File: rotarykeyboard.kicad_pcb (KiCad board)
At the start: 2 copper layers, 53 parts, among them J101 Breakout, J102 Cortex Debug, J301 USB_C_Receptacle_USB2.0, SW101 RotaryEncoder, SW102 KBPush, SW103 RESET, U101 ATSAMDA1E14B-ABT, U201 QS6K1FRATR, U202 LTP-3784E, U203 PCA9685PW, U301 FTZU6.2ET148, U302 XC9265A331MR-G

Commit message: finish routing(?)
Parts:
- added REF**: MountingHole_2.2mm_M2_ISO7380, MountingHole:MountingHole_2.2mm_M2_ISO7380, F.Cu at (106.7, 40.6)
- added REF**: MountingHole_2.2mm_M2_ISO7380, MountingHole:MountingHole_2.2mm_M2_ISO7380, F.Cu at (106.7, 113.0)
- added REF**: MountingHole_2.2mm_M2_ISO7380, MountingHole:MountingHole_2.2mm_M2_ISO7380, F.Cu at (62.2, 40.6)
- added REF**: MountingHole_2.2mm_M2_ISO7380, MountingHole:MountingHole_2.2mm_M2_ISO7380, F.Cu at (62.2, 113.0)
- moved R203 25.2 mm to (63.8, 99.3), turned to -90 degrees
- moved R204 20.9 mm to (63.8, 94.7), turned to -90 degrees
- moved R212 18.8 mm to (81.5, 85.3), turned to -90 degrees
- moved R215 15.3 mm to (78.0, 89.9), turned to -90 degrees
- moved R210 14.2 mm to (81.5, 80.8), turned to -90 degrees
- moved R207 12.7 mm to (63.8, 89.9), turned to -90 degrees
- moved R208 11.1 mm to (63.8, 85.3), turned to -90 degrees
- moved R214 10.9 mm to (81.5, 89.9), turned to -90 degrees
- moved R213 10.7 mm to (78.0, 85.3), turned to -90 degrees
- moved U203 10.4 mm to (70.9, 79.2), turned to 0 degrees
- moved R209 9.77 mm to (67.3, 89.9), turned to -90 degrees
- moved U201 9.51 mm to (89.3, 90.4), turned to -90 degrees
- moved R205 8.13 mm to (63.8, 74.4), turned to -90 degrees
- moved R216 7.28 mm to (74.4, 89.9), turned to -90 degrees
- moved R211 6.13 mm to (78.0, 80.8), turned to -90 degrees
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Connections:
- R203 pad 1: Net-(R203-Pad1) -> Net-(U203-Pad6)
- R203 pad 2: Net-(R203-Pad2) -> Net-(U202-Pad1)
- R204 pad 1: Net-(R204-Pad1) -> Net-(U203-Pad7)
- R204 pad 2: Net-(R204-Pad2) -> Net-(U202-Pad2)
- R205 pad 1: Net-(R205-Pad1) -> Net-(U203-Pad8)
- R206 pad 1: Net-(R206-Pad1) -> Net-(U203-Pad9)
- R206 pad 2: Net-(R206-Pad2) -> Net-(U202-Pad5)
- R207 pad 1: Net-(R207-Pad1) -> Net-(U203-Pad10)
- R207 pad 2: Net-(R207-Pad2) -> Net-(U202-Pad6)
- R208 pad 1: Net-(R208-Pad1) -> Net-(U203-Pad11)
- R209 pad 1: Net-(R209-Pad1) -> Net-(U203-Pad12)
- U202 pad 1: Net-(R203-Pad1) -> Net-(U202-Pad1)
- U202 pad 2: Net-(R204-Pad1) -> Net-(U202-Pad2)
- U202 pad 4: Net-(R205-Pad1) -> Net-(R205-Pad2)
- U202 pad 5: Net-(R206-Pad1) -> Net-(U202-Pad5)
- U202 pad 6: Net-(R207-Pad1) -> Net-(U202-Pad6)
- U202 pad 7: Net-(R208-Pad1) -> Net-(R208-Pad2)
- U202 pad 8: Net-(R209-Pad1) -> Net-(R209-Pad2)
- U203 pad 10: Net-(R207-Pad2) -> Net-(U203-Pad10)
- U203 pad 11: Net-(R208-Pad2) -> Net-(U203-Pad11)
- U203 pad 12: Net-(R209-Pad2) -> Net-(U203-Pad12)
- U203 pad 6: Net-(R203-Pad2) -> Net-(U203-Pad6)
- U203 pad 7: Net-(R204-Pad2) -> Net-(U203-Pad7)
- U203 pad 8: Net-(R205-Pad2) -> Net-(U203-Pad8)
- U203 pad 9: Net-(R206-Pad2) -> Net-(U203-Pad9)
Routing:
- net Net-(R205-Pad2): track 0.00 -> 47.7 mm, vias 0 -> 1
- net Net-(U202-Pad5): track 0.00 -> 44.9 mm, vias 0 -> 1
- net Net-(R208-Pad2): track 0.00 -> 41.2 mm, vias 0 -> 1
- net GND: track 170.2 -> 211.0 mm, vias 9 -> 12
- net Net-(R217-Pad2): track 0.00 -> 39.1 mm, vias 0 -> 1
- net Net-(R209-Pad2): track 0.00 -> 37.3 mm, vias 0 -> 1
- net Net-(U202-Pad6): track 0.00 -> 34.5 mm, vias 0 -> 1
- net Net-(R216-Pad2): track 0.00 -> 33.3 mm
- net Net-(R211-Pad2): track 0.00 -> 31.0 mm, vias 0 -> 1
- net Net-(U203-Pad6): track 0.00 -> 29.8 mm
- net Net-(R210-Pad2): track 0.00 -> 29.0 mm
- net Net-(U201-Pad4): track 32.0 -> 5.27 mm
- net Net-(U203-Pad7): track 0.00 -> 24.4 mm
- net Net-(R101-Pad2): track 30.0 -> 53.3 mm
- net Net-(U202-Pad2): track 0.00 -> 22.1 mm, vias 0 -> 1
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- added copper zone on B.Cu, net +3V3
- removed copper zone on F.Cu, net +5V
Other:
- board outline added: 49.5 x 77.5 mm
- board text removed: "roter LED-driveren 90 grader flytt displaymotstandene til hver sin side av driveren"

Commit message: replace out of stock components
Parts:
- added C201: 0.1u, Capacitor_SMD:C_0805_2012Metric, F.Cu at (133.3, 82.5)
- added R210: 100k, Resistor_SMD:R_0805_2012Metric, F.Cu at (137.8, 82.5)
- added R219: 6k8, Resistor_SMD:R_0805_2012Metric, F.Cu at (133.3, 85.5)
- U203: value PCA9685PW -> IS32FL3238
- U301: value FTZU6.2ET148 -> BZA856AVL; footprint FTZU6.2ET148:FTZU6.2ET148 -> BZA856AVL:BZA856AVL
- moved U301 45.2 mm to (117.9, 86.9), turned to 0 degrees
- renumbered C106 to C101, C107 to C102, C101 to C103, C102 to C104, C103 to C105, C104 to C106, C105 to C107, R210 to R211, R211 to R212, R212 to R213, R213 to R214, R214 to R215, R215 to R216, R216 to R217, R217 to R218, GND to TP301, +3V3 to TP302
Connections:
- R203 pad 1: Net-(U203-Pad6) -> Net-(R203-Pad1)
- R204 pad 1: Net-(U203-Pad7) -> Net-(R204-Pad1)
- R205 pad 1: Net-(U203-Pad8) -> Net-(R205-Pad1)
- R206 pad 1: Net-(U203-Pad9) -> Net-(R206-Pad1)
- R207 pad 1: Net-(U203-Pad10) -> Net-(R207-Pad1)
- R208 pad 1: Net-(U203-Pad11) -> Net-(R208-Pad1)
- R209 pad 1: Net-(U203-Pad12) -> Net-(R209-Pad1)
- R217 pad 1: Net-(R216-Pad1) (its old number) -> Net-(R217-Pad1)
- R218 pad 1: Net-(R217-Pad1) -> Net-(R218-Pad1)
- U101 pad 13: /Segment display/~OE -> /Segment display/EN
- U201 pad 2: GND -> Net-(U201-Pad2)
- U201 pad 4: Net-(U201-Pad4) -> +3V3
- U201 pad 5: GND -> Net-(U201-Pad5)
- U201 pad 6: Net-(U201-Pad6) -> +3V3
- U202 pad 11: Net-(U201-Pad4) -> Net-(U201-Pad2)
- U202 pad 16: Net-(U201-Pad6) -> Net-(U201-Pad5)
- U203 pad 1: +3V3 -> (no net)
- U203 pad 10: Net-(U203-Pad10) -> Net-(R208-Pad1)
- U203 pad 11: Net-(U203-Pad11) -> Net-(R209-Pad1)
- U203 pad 12: Net-(U203-Pad12) -> Net-(R218-Pad1)
- U203 pad 15: Net-(R216-Pad1) (its old number) -> GND
- U203 pad 2: GND -> Net-(R219-Pad1)
- U203 pad 23: /Segment display/~OE -> unconnected-(U203-Pad23)
- U203 pad 24: GND -> unconnected-(U203-Pad24)
- U203 pad 25: GND -> /Segment display/EN
- U203 pad 26: /Segment display/SCL -> +3V3
- U203 pad 27: /Segment display/SDA -> +3V3
- U203 pad 28: +3V3 -> GND
- U203 pad 3: +3V3 -> /Segment display/SDA
- U203 pad 4: GND -> /Segment display/SCL
- U203 pad 5: +3V3 -> Net-(R203-Pad1)
- U203 pad 6: Net-(U203-Pad6) -> Net-(R204-Pad1)
- U203 pad 7: Net-(U203-Pad7) -> Net-(R205-Pad1)
- U203 pad 8: Net-(U203-Pad8) -> Net-(R206-Pad1)
- U203 pad 9: Net-(U203-Pad9) -> Net-(R207-Pad1)
- U301 pad 1: /USB & Power/USB_D+ -> unconnected-(U301-Pad1)
- U301 pad 2: /USB & Power/USB_D- -> Net-(C301-Pad1)
- U301 pad 4: Net-(C301-Pad1) -> /USB & Power/USB_D-
- U301 pad 5: unconnected-(U301-Pad5) -> /USB & Power/USB_D+
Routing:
- net unconnected-(U203-Pad23): track 0.00 -> 32.7 mm
- net /Segment display/~OE: track 32.7 -> 0.00 mm
- net Net-(U203-Pad6): track 29.8 -> 0.00 mm
- net Net-(R203-Pad1): track 0.00 -> 29.8 mm
- net Net-(U203-Pad7): track 24.4 -> 0.00 mm
- net Net-(R205-Pad1): track 0.00 -> 24.4 mm
- net Net-(U201-Pad6): track 20.7 -> 0.00 mm, vias 2 -> 0
- net Net-(U201-Pad5): track 0.00 -> 20.7 mm, vias 0 -> 2
- net Net-(U203-Pad12): track 12.9 -> 0.00 mm, vias 2 -> 0
- net Net-(R218-Pad1): track 0.00 -> 12.9 mm, vias 0 -> 2
- net Net-(U203-Pad10): track 12.6 -> 0.00 mm
- net Net-(R208-Pad1): track 0.00 -> 12.6 mm
- net Net-(U203-Pad8): track 12.4 -> 0.00 mm
- net Net-(R206-Pad1): track 0.00 -> 12.4 mm
- net Net-(U203-Pad9): track 8.09 -> 0.00 mm
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
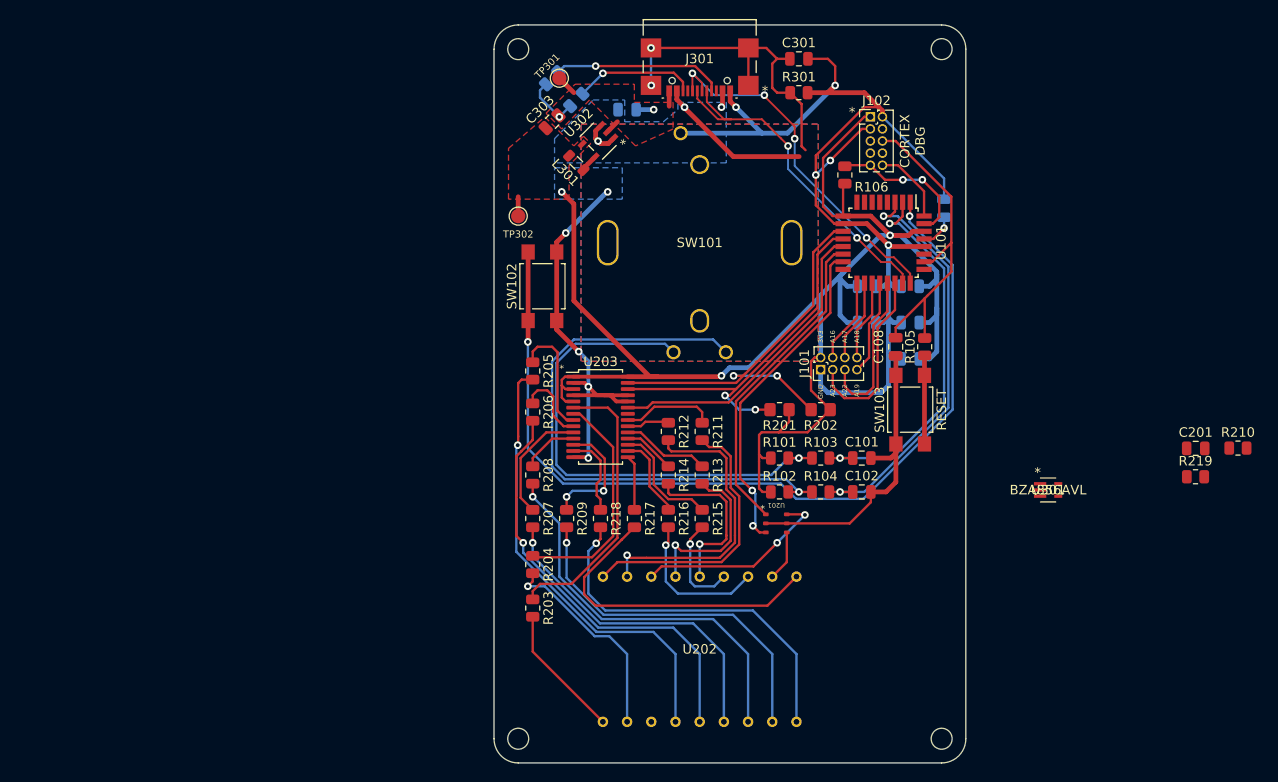
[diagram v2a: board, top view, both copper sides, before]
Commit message: reroute new components
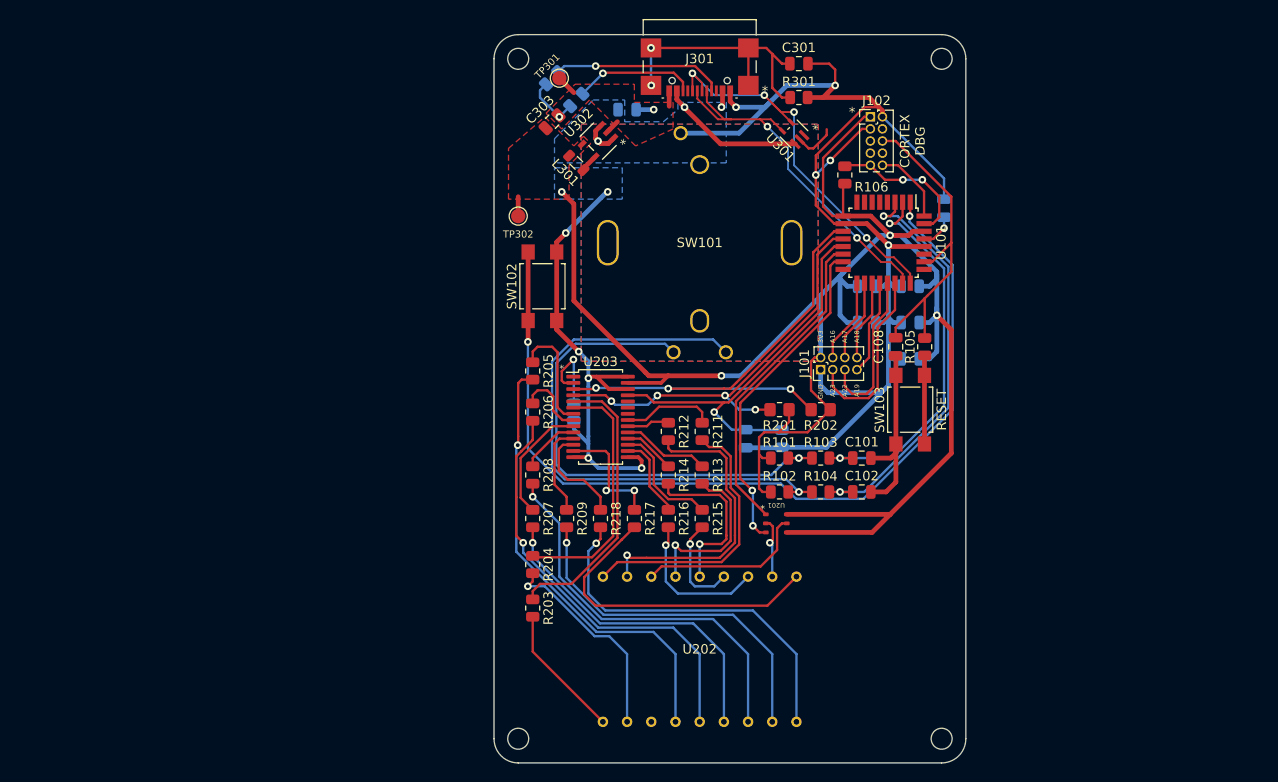
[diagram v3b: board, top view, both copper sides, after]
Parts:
- C201, R210: moved to B.Cu
- R219: value 6k8 -> 10k; moved to B.Cu
- moved R219 65.6 mm to (68.1, 78.7), turned to -90 degrees
- moved R210 47.9 mm to (89.9, 81.5), turned to -90 degrees
- moved C201 47.3 mm to (86.1, 81.5), turned to -90 degrees
- moved U301 45.9 mm to (91.2, 49.5), turned to -45 degrees
- moved REF** 1.02 mm to (106.7, 41.7)
- moved REF** 1.02 mm to (62.2, 41.7)
- moved C301 0.51 mm to (91.7, 42.2)
- moved R301 0.51 mm to (91.7, 45.7)
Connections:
- U203 pad 26: +3V3 -> GND
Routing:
- net /Segment display/EN: track 0.00 -> 42.2 mm, vias 0 -> 1
- net +3V3: track 163.7 -> 200.0 mm, vias 3 -> 4
- net unconnected-(U203-Pad23): track 32.7 -> 0.00 mm
- net Net-(R204-Pad1): track 0.00 -> 26.4 mm
- net Net-(R205-Pad1): track 24.4 -> 11.9 mm
- net /Segment display/SDA: track 43.5 -> 54.8 mm, vias 2 -> 3
- net Net-(R219-Pad1): track 0.00 -> 8.66 mm, vias 0 -> 1
- net Net-(R208-Pad1): track 12.6 -> 6.24 mm
- net /Segment display/SCL: track 39.2 -> 44.6 mm, vias 2 -> 4
- net Net-(R206-Pad1): track 12.4 -> 7.52 mm
- net Net-(R207-Pad1): track 8.09 -> 12.9 mm
- net GND: track 216.9 -> 220.9 mm, vias 12 -> 13
- net Net-(R217-Pad1): track 8.79 -> 12.8 mm, vias 0 -> 2
- net /USB & Power/USB_D+: track 39.2 -> 43.0 mm
- net Net-(R209-Pad1): track 5.97 -> 9.67 mm
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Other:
- board size 49.5 x 77.5 mm -> 49.5 x 76.5 mm

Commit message: påske
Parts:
- removed R203, R204, R205, R206, R207, R208, R209, R211, R212, R213, R214, R215, R216, R217, R218: 330, Resistor_SMD:R_0805_2012Metric
- U202: value LTP-3784E -> XAMR14A2
- moved U201 12.7 mm to (80.3, 81.5), turned to 180 degrees
- moved U202 3.56 mm to (81.3, 100.1)
- moved REF** 2.16 mm to (106.7, 110.9)
- moved REF** 2.16 mm to (62.2, 110.9)
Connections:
- U202 pad 1: Net-(R203-Pad2) -> Net-(U203-Pad5)
- U202 pad 10: Net-(R217-Pad2) -> Net-(U203-Pad13)
- U202 pad 11: Net-(U201-Pad2) -> Net-(U201-Pad5)
- U202 pad 12: Net-(R216-Pad2) -> Net-(U203-Pad16)
- U202 pad 13: Net-(R215-Pad2) -> Net-(U203-Pad17)
- U202 pad 14: Net-(R214-Pad2) -> Net-(U203-Pad18)
- U202 pad 15: Net-(R213-Pad2) -> Net-(U203-Pad19)
- U202 pad 16: Net-(U201-Pad5) -> Net-(U201-Pad2)
- U202 pad 17: Net-(R212-Pad2) -> Net-(U203-Pad20)
- U202 pad 18: Net-(R211-Pad2) -> Net-(U203-Pad21)
- U202 pad 2: Net-(R204-Pad2) -> Net-(U203-Pad6)
- U202 pad 4: Net-(R205-Pad2) -> Net-(U203-Pad7)
- U202 pad 5: Net-(R206-Pad2) -> Net-(U203-Pad8)
- U202 pad 6: Net-(R207-Pad2) -> Net-(U203-Pad9)
- U202 pad 7: Net-(R208-Pad2) -> Net-(U203-Pad10)
- U202 pad 8: Net-(R209-Pad2) -> Net-(U203-Pad11)
- U202 pad 9: Net-(R218-Pad2) -> Net-(U203-Pad12)
- U203 pad 10: Net-(R208-Pad1) -> Net-(U203-Pad10)
- U203 pad 11: Net-(R209-Pad1) -> Net-(U203-Pad11)
- U203 pad 12: Net-(R218-Pad1) -> Net-(U203-Pad12)
- U203 pad 13: Net-(R217-Pad1) -> Net-(U203-Pad13)
- U203 pad 16: Net-(R216-Pad1) -> Net-(U203-Pad16)
- U203 pad 17: Net-(R215-Pad1) -> Net-(U203-Pad17)
- U203 pad 18: Net-(R214-Pad1) -> Net-(U203-Pad18)
- U203 pad 19: Net-(R213-Pad1) -> Net-(U203-Pad19)
- U203 pad 20: Net-(R212-Pad1) -> Net-(U203-Pad20)
- U203 pad 21: Net-(R211-Pad1) -> Net-(U203-Pad21)
- U203 pad 5: Net-(R203-Pad1) -> Net-(U203-Pad5)
- U203 pad 6: Net-(R204-Pad1) -> Net-(U203-Pad6)
- U203 pad 7: Net-(R205-Pad1) -> Net-(U203-Pad7)
- U203 pad 8: Net-(R206-Pad1) -> Net-(U203-Pad8)
- U203 pad 9: Net-(R207-Pad1) -> Net-(U203-Pad9)
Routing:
- net Net-(R205-Pad2): track 47.7 -> 0.00 mm, vias 1 -> 0
- net Net-(U203-Pad12): track 0.00 -> 46.6 mm
- net Net-(U203-Pad11): track 0.00 -> 45.5 mm
- net Net-(R206-Pad2): track 44.9 -> 0.00 mm, vias 1 -> 0
- net Net-(U203-Pad13): track 0.00 -> 44.4 mm
- net Net-(U203-Pad10): track 0.00 -> 44.3 mm
- net Net-(U203-Pad9): track 0.00 -> 43.2 mm
- net Net-(U203-Pad8): track 0.00 -> 42.0 mm
- net Net-(R208-Pad2): track 41.2 -> 0.00 mm, vias 1 -> 0
- net Net-(U203-Pad7): track 0.00 -> 40.9 mm
- net Net-(R218-Pad2): track 39.1 -> 0.00 mm, vias 1 -> 0
- net Net-(R209-Pad2): track 37.3 -> 0.00 mm, vias 1 -> 0
- net Net-(U203-Pad6): track 0.00 -> 37.2 mm
- net Net-(U203-Pad5): track 0.00 -> 36.0 mm
- net Net-(R207-Pad2): track 34.5 -> 0.00 mm, vias 1 -> 0
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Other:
- board size 49.5 x 76.5 mm -> 49.5 x 74.3 mm

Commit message: final component changes
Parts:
- U202: value XAMR14A2 -> HDSP-A22C
- renumbered R210 to R203, R219 to R204
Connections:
- R204 pad 1: Net-(R219-Pad1) -> Net-(R204-Pad1)
- U202 pad 1: Net-(U203-Pad5) -> Net-(U202-Pad1)
- U202 pad 10: Net-(U203-Pad13) -> Net-(U202-Pad10)
- U202 pad 12: Net-(U203-Pad16) -> Net-(U202-Pad12)
- U202 pad 13: Net-(U203-Pad17) -> Net-(U202-Pad13)
- U202 pad 14: Net-(U203-Pad18) -> Net-(U202-Pad14)
- U202 pad 15: Net-(U203-Pad19) -> Net-(U202-Pad15)
- U202 pad 17: Net-(U203-Pad20) -> Net-(U202-Pad17)
- U202 pad 18: Net-(U203-Pad21) -> Net-(U202-Pad18)
- U202 pad 2: Net-(U203-Pad6) -> Net-(U202-Pad2)
- U202 pad 4: Net-(U203-Pad7) -> Net-(U202-Pad4)
- U202 pad 5: Net-(U203-Pad8) -> Net-(U202-Pad5)
- U202 pad 6: Net-(U203-Pad9) -> Net-(U202-Pad6)
- U202 pad 7: Net-(U203-Pad10) -> Net-(U202-Pad7)
- U202 pad 8: Net-(U203-Pad11) -> Net-(U202-Pad8)
- U202 pad 9: Net-(U203-Pad12) -> Net-(U202-Pad9)
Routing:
- net Net-(R219-Pad1): track 8.66 -> 0.00 mm, vias 1 -> 0
- net Net-(R204-Pad1): track 0.00 -> 8.66 mm, vias 0 -> 1

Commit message: production pcb
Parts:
- renumbered TP302 to +3V3, TP301 to GND
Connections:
- U203 pad 10: Net-(U203-Pad10) -> Net-(U202-Pad7)
- U203 pad 11: Net-(U203-Pad11) -> Net-(U202-Pad8)
- U203 pad 12: Net-(U203-Pad12) -> Net-(U202-Pad9)
- U203 pad 13: Net-(U203-Pad13) -> Net-(U202-Pad10)
- U203 pad 16: Net-(U203-Pad16) -> Net-(U202-Pad12)
- U203 pad 17: Net-(U203-Pad17) -> Net-(U202-Pad13)
- U203 pad 18: Net-(U203-Pad18) -> Net-(U202-Pad14)
- U203 pad 19: Net-(U203-Pad19) -> Net-(U202-Pad15)
- U203 pad 2: Net-(R219-Pad1) -> Net-(R204-Pad1)
- U203 pad 20: Net-(U203-Pad20) -> Net-(U202-Pad17)
- U203 pad 21: Net-(U203-Pad21) -> Net-(U202-Pad18)
- U203 pad 5: Net-(U203-Pad5) -> Net-(U202-Pad1)
- U203 pad 6: Net-(U203-Pad6) -> Net-(U202-Pad2)
- U203 pad 7: Net-(U203-Pad7) -> Net-(U202-Pad4)
- U203 pad 8: Net-(U203-Pad8) -> Net-(U202-Pad5)
- U203 pad 9: Net-(U203-Pad9) -> Net-(U202-Pad6)
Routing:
- net GND: track 221.3 -> 171.2 mm, vias 13 -> 14
- net +3V3: track 206.5 -> 158.6 mm
- net Net-(U203-Pad12): track 46.6 -> 0.00 mm
- net Net-(U202-Pad9): track 0.00 -> 46.6 mm
- net Net-(U203-Pad11): track 45.5 -> 0.00 mm
- net Net-(U202-Pad8): track 0.00 -> 45.5 mm
- net Net-(U203-Pad13): track 44.4 -> 0.00 mm
- net Net-(U202-Pad10): track 0.00 -> 44.4 mm
- net Net-(U203-Pad10): track 44.3 -> 0.00 mm
- net Net-(U202-Pad7): track 0.00 -> 44.3 mm
- net Net-(U203-Pad9): track 43.2 -> 0.00 mm
- net Net-(U202-Pad6): track 0.00 -> 43.2 mm
- net Net-(U203-Pad8): track 42.0 -> 0.00 mm
- net Net-(U202-Pad5): track 0.00 -> 42.0 mm
- net Net-(U203-Pad7): track 40.9 -> 0.00 mm
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- added copper zone on B.Cu, net GND
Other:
- board text added: "JLCJLCJLCJLC"
- board text added: "halworsen"
